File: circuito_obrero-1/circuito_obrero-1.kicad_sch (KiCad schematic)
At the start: 13 parts, among them J1 Conn_01x03_Pin, J10 Conn_01x05, J2 Conn_01x03_Pin, J3 Conn_01x03_Pin, J4 Conn_01x03_Pin, J5 Conn_01x03_Pin, J6 Conn_01x03_Pin, J7 Conn_01x03_Pin, J8 Conn_01x03_Pin, J9 Conn_01x05, U1 74HC165, U2 74HC165, U3 74HC165

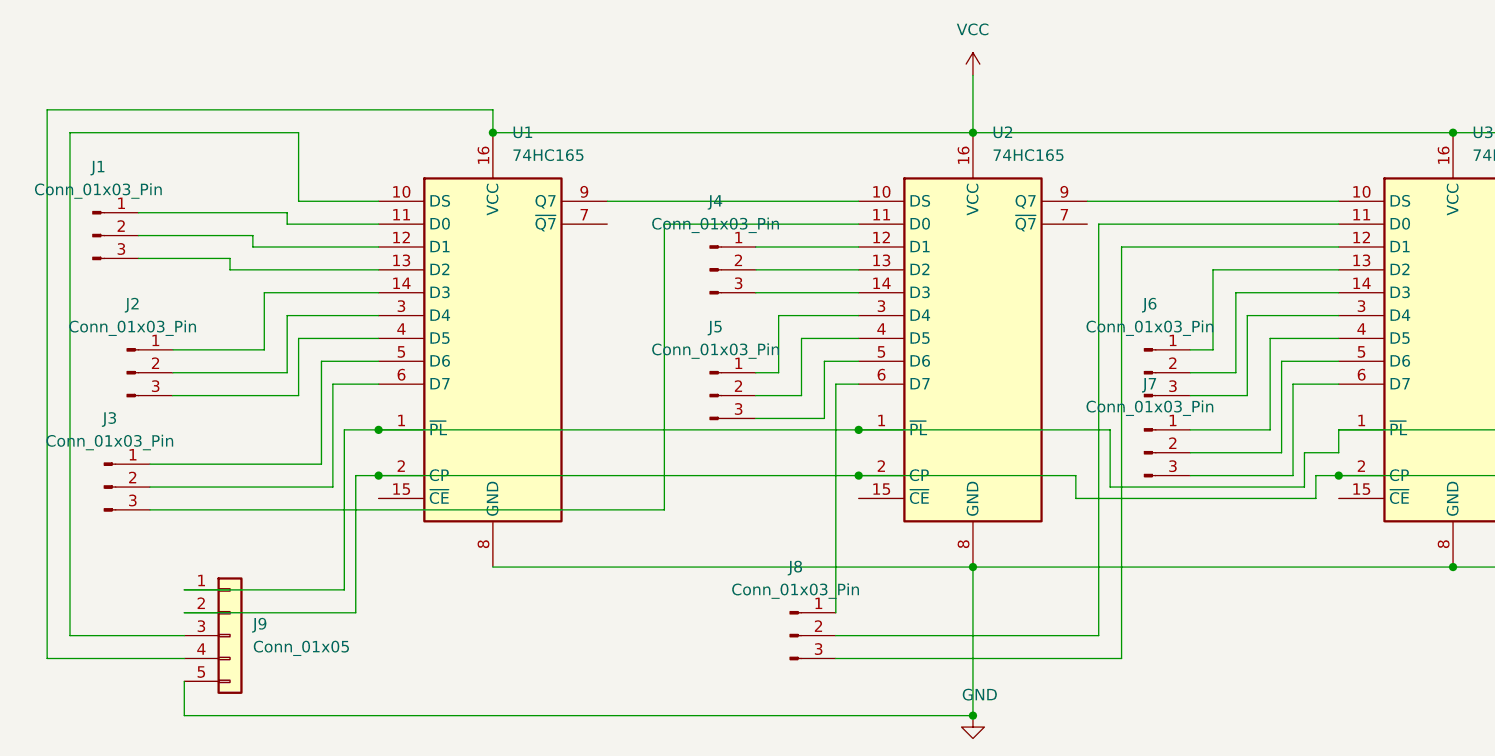
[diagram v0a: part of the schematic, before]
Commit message: sumando resistencias al circuito
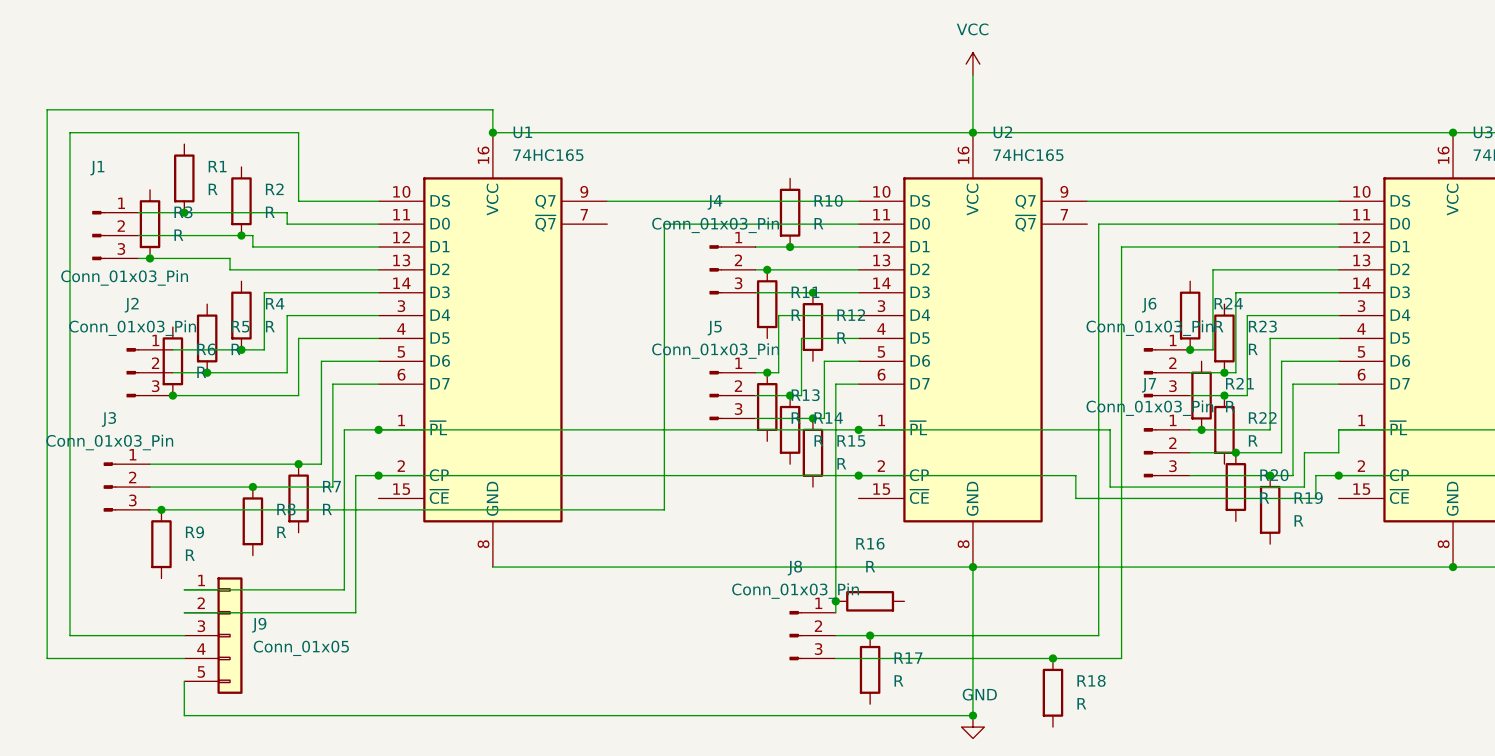
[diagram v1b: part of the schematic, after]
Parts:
- added R1, R10, R11, R12, R13, R14, R15, R16, R17, R18, R19, R2, R20, R21, R22, R23, R24, R3, R4, R5, R6, R7, R8, R9: R, symbol Device:R
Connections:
- net at J6.1 (Pin_1), U3.13 (D2): now also R24.2
- net at J6.2 (Pin_2), U3.14 (D3): now also R23.2
- net at J6.3 (Pin_3), U3.3 (D4): now also R22.1
- net at J3.1 (Pin_1), U1.5 (D6): now also R7.1
- net at J3.2 (Pin_2), U1.6 (D7): now also R8.1
- net at J3.3 (Pin_3), U2.11 (D0): now also R9.1
- net at J1.1 (Pin_1), U1.11 (D0): now also R1.2
- net at J1.2 (Pin_2), U1.12 (D1): now also R2.2
- net at J1.3 (Pin_3), U1.13 (D2): now also R3.2
- net at J2.1 (Pin_1), U1.14 (D3): now also R4.2
- net at J2.2 (Pin_2), U1.3 (D4): now also R5.2
- net at J2.3 (Pin_3), U1.4 (D5): now also R6.2
- net at J8.2 (Pin_2), U3.11 (D0): now also R17.1
- net at J8.3 (Pin_3), U3.12 (D1): now also R18.1
- net at J7.1 (Pin_1), U3.4 (D5): now also R21.2
- net at J7.2 (Pin_2), U3.5 (D6): now also R20.1
- net at J7.3 (Pin_3), U3.6 (D7): now also R19.1
- net at J8.1 (Pin_1), U2.6 (D7): now also R16.1
- net at J4.1 (Pin_1), U2.12 (D1): now also R10.2
- net at J4.2 (Pin_2), U2.13 (D2): now also R11.1
- net at J4.3 (Pin_3), U2.14 (D3): now also R12.1
- net at J5.1 (Pin_1), U2.3 (D4): now also R13.1
- net at J5.2 (Pin_2), U2.4 (D5): now also R14.1
- net at J5.3 (Pin_3), U2.5 (D6): now also R15.1

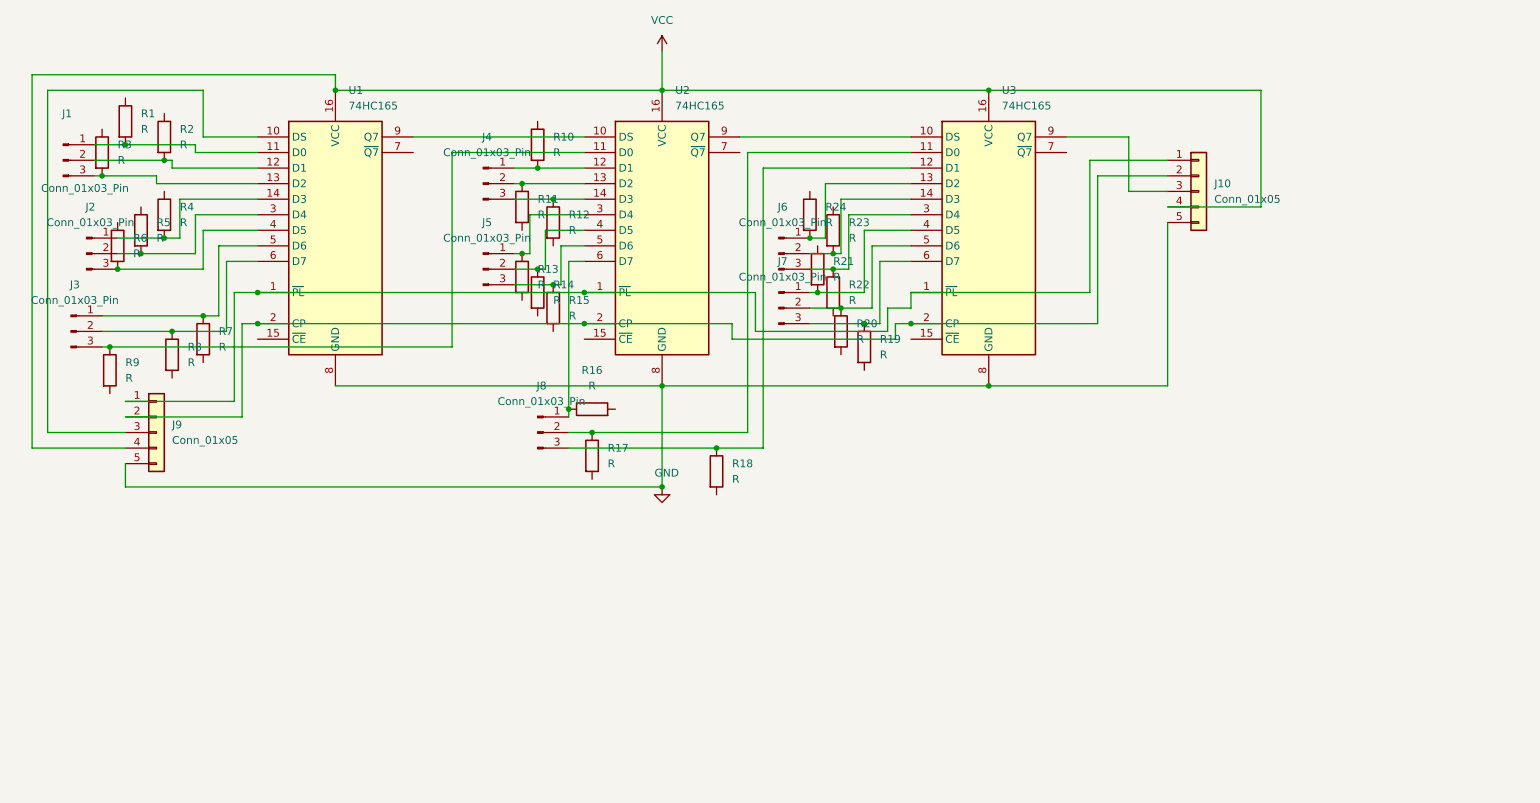
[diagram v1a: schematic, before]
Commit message: agregadas las resis al circuito
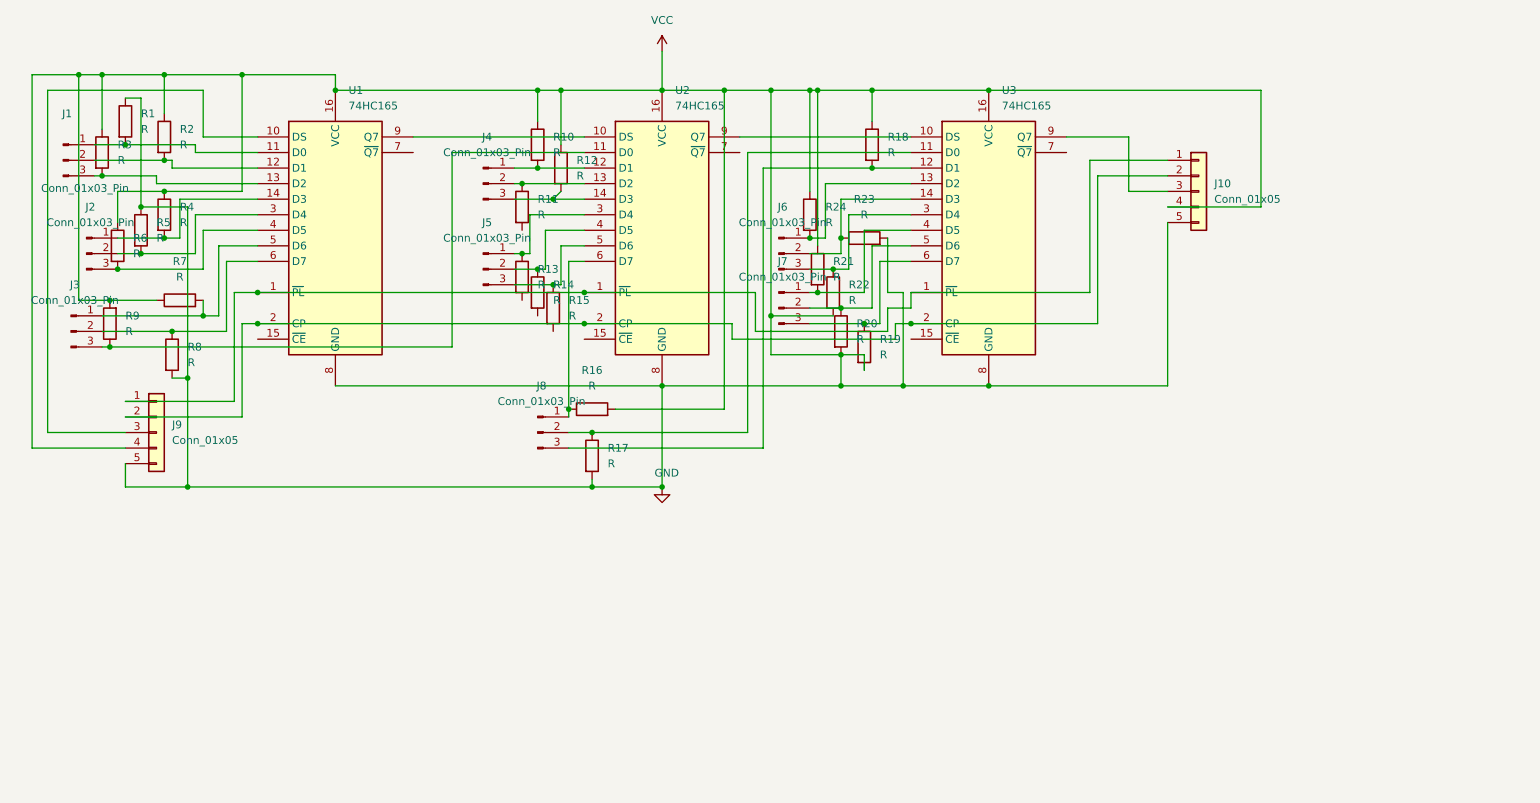
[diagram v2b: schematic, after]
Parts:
- R1, R10, R11, R12, R13, R14, R15, R16, R17, R18, R19, R2, R20, R21, R22, R23, R24, R3, R4, R5, R6, R7, R8, R9: footprint (none) -> Resistor_THT:R_Axial_DIN0204_L3.6mm_D1.6mm_P5.08mm_Horizontal
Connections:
- net VCC is gone; now on net GND: J10.4 (Pin_4), J9.4 (Pin_4), U1.16 (VCC), U2.16 (VCC), U3.16 (VCC)
- net GND: now also R1.1, R10.1, R12.1, R16.2, R17.2, R18.1, R19.2, R2.1, R20.2, R21.1, R22.2, R23.2, R24.1, R3.1, R4.1, R5.1, R6.1, R7.1, R8.2, R9.2
- net at J6.2 (Pin_2), U3.14 (D3): now also R23.1; no longer R23.2
- net at J3.1 (Pin_1), U1.5 (D6): now also R7.2; no longer R7.1
- net at J8.3 (Pin_3), U3.12 (D1): now also R18.2; no longer R18.1
- net at J4.3 (Pin_3), U2.14 (D3): now also R12.2; no longer R12.1
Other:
- moved on the sheet: R12, R18, R23, R7, R9

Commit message: vcc funcional
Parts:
- added J11: Conn_01x05_Socket, Connector_JST:JST_EH_B5B-EH-A_1x05_P2.50mm_Vertical, symbol Connector:Conn_01x05_Socket
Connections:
- net GND: now also J11.5 (Pin_5); no longer J10.4 (Pin_4), J9.4 (Pin_4)
- net at J10.1 (Pin_1), J9.1 (Pin_1), U1.1 (~{PL})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: now also J11.1 (Pin_1)
- net at J10.2 (Pin_2), J9.2 (Pin_2), U1.2 (CP)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: now also J11.2 (Pin_2)
- net at J10.3 (Pin_3), U3.9 (Q7): now also J11.3 (Pin_3)
- new net +5V: J11.4 (Pin_4)
- new net VCC: J10.4 (Pin_4), J9.4 (Pin_4)
- no-connect marks 0 -> 6

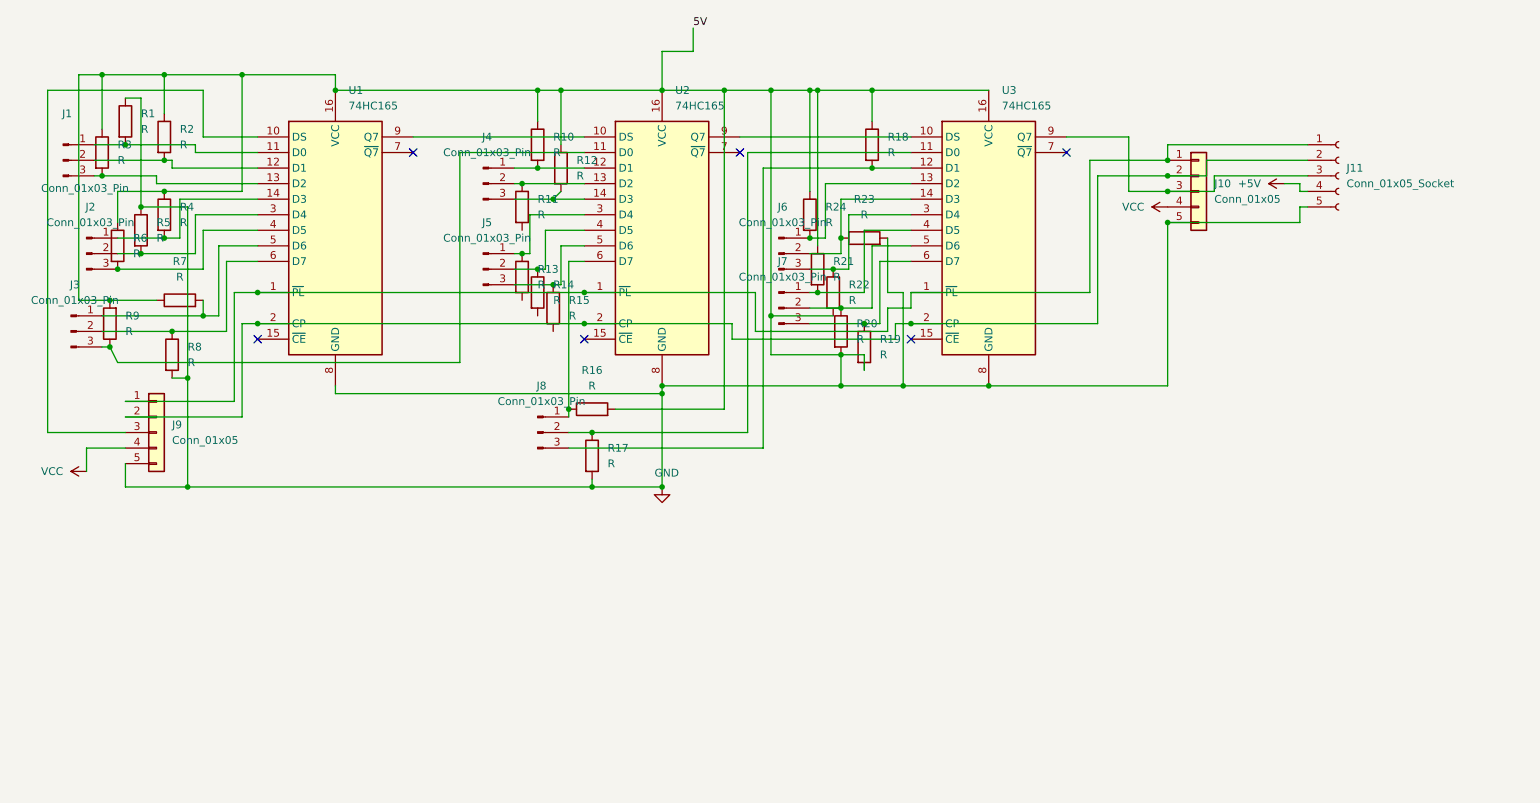
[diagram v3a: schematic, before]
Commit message: acomodando resistencias (revisar si es pull up o pull down el btn y los encoders)
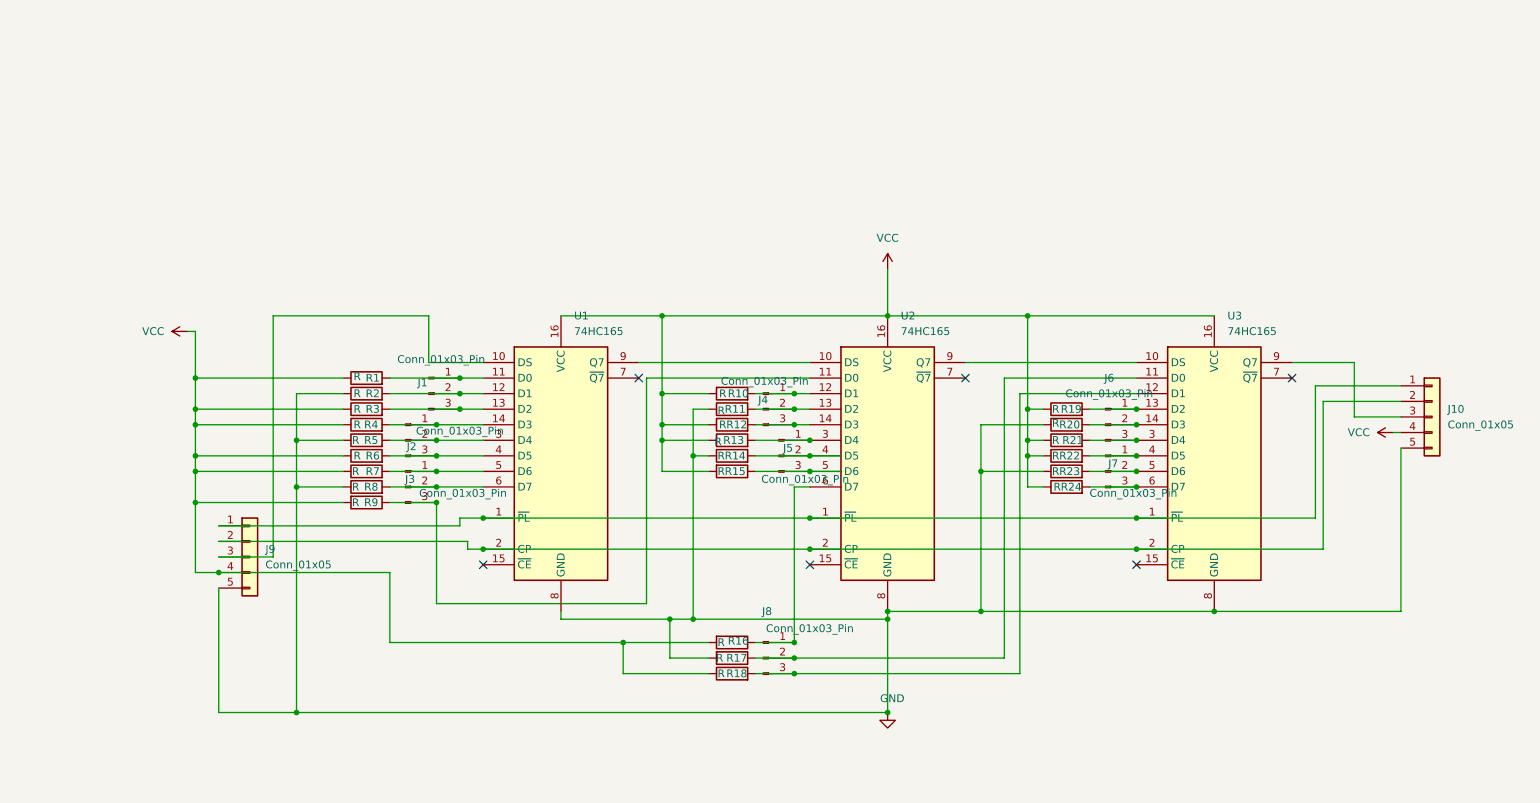
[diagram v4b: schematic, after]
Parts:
- removed J11: Conn_01x05_Socket, Connector_JST:JST_EH_B5B-EH-A_1x05_P2.50mm_Vertical, symbol Connector:Conn_01x05_Socket
- U1, U2, U3: footprint Package_DIP:CERDIP-14_W7.62mm_SideBrazed_Socket -> Package_DIP:CERDIP-16_W7.62mm_SideBrazed_LongPads_Socket
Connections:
- net GND: now also R11.1, R14.1, R20.1, R23.1, R8.1; no longer R1.1, R10.1, R12.1, R16.2, R18.1, R19.2, R20.2, R21.1, R22.2, R23.2, R24.1, R3.1, R4.1, R6.1, R7.1, R8.2, R9.2, U1.16 (VCC), U2.16 (VCC), U3.16 (VCC)
- net VCC: now also R1.1, R10.1, R12.1, R13.1, R15.2, R16.2, R18.1, R19.1, R21.1, R22.1, R24.1, R3.1, R4.1, R6.1, R7.1, R9.2, U1.16 (VCC), U2.16 (VCC), U3.16 (VCC)
- net at J6.1 (Pin_1), U3.13 (D2): now also R19.2; no longer R24.2
- net at J6.2 (Pin_2), U3.14 (D3): now also R20.2; no longer R23.1
- net at J6.3 (Pin_3), U3.3 (D4): now also R21.2; no longer R22.1
- net at J3.2 (Pin_2), U1.6 (D7): now also R8.2; no longer R8.1
- net at J7.3 (Pin_3), U3.6 (D7): now also R24.2; no longer R19.1
- net at J7.1 (Pin_1), U3.4 (D5): now also R22.2; no longer R21.2
- net at J7.2 (Pin_2), U3.5 (D6): now also R23.2; no longer R20.1
- net at J5.1 (Pin_1), U2.3 (D4): now also R13.2; no longer R13.1
- net at J4.2 (Pin_2), U2.13 (D2): now also R11.2; no longer R11.1
- net at J5.2 (Pin_2), U2.4 (D5): now also R14.2; no longer R14.1
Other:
- moved on the sheet: J1, J10, J2, J3, J4, J5, J6, J7, J8, J9, R1, R10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
